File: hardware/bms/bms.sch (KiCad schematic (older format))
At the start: 159 parts

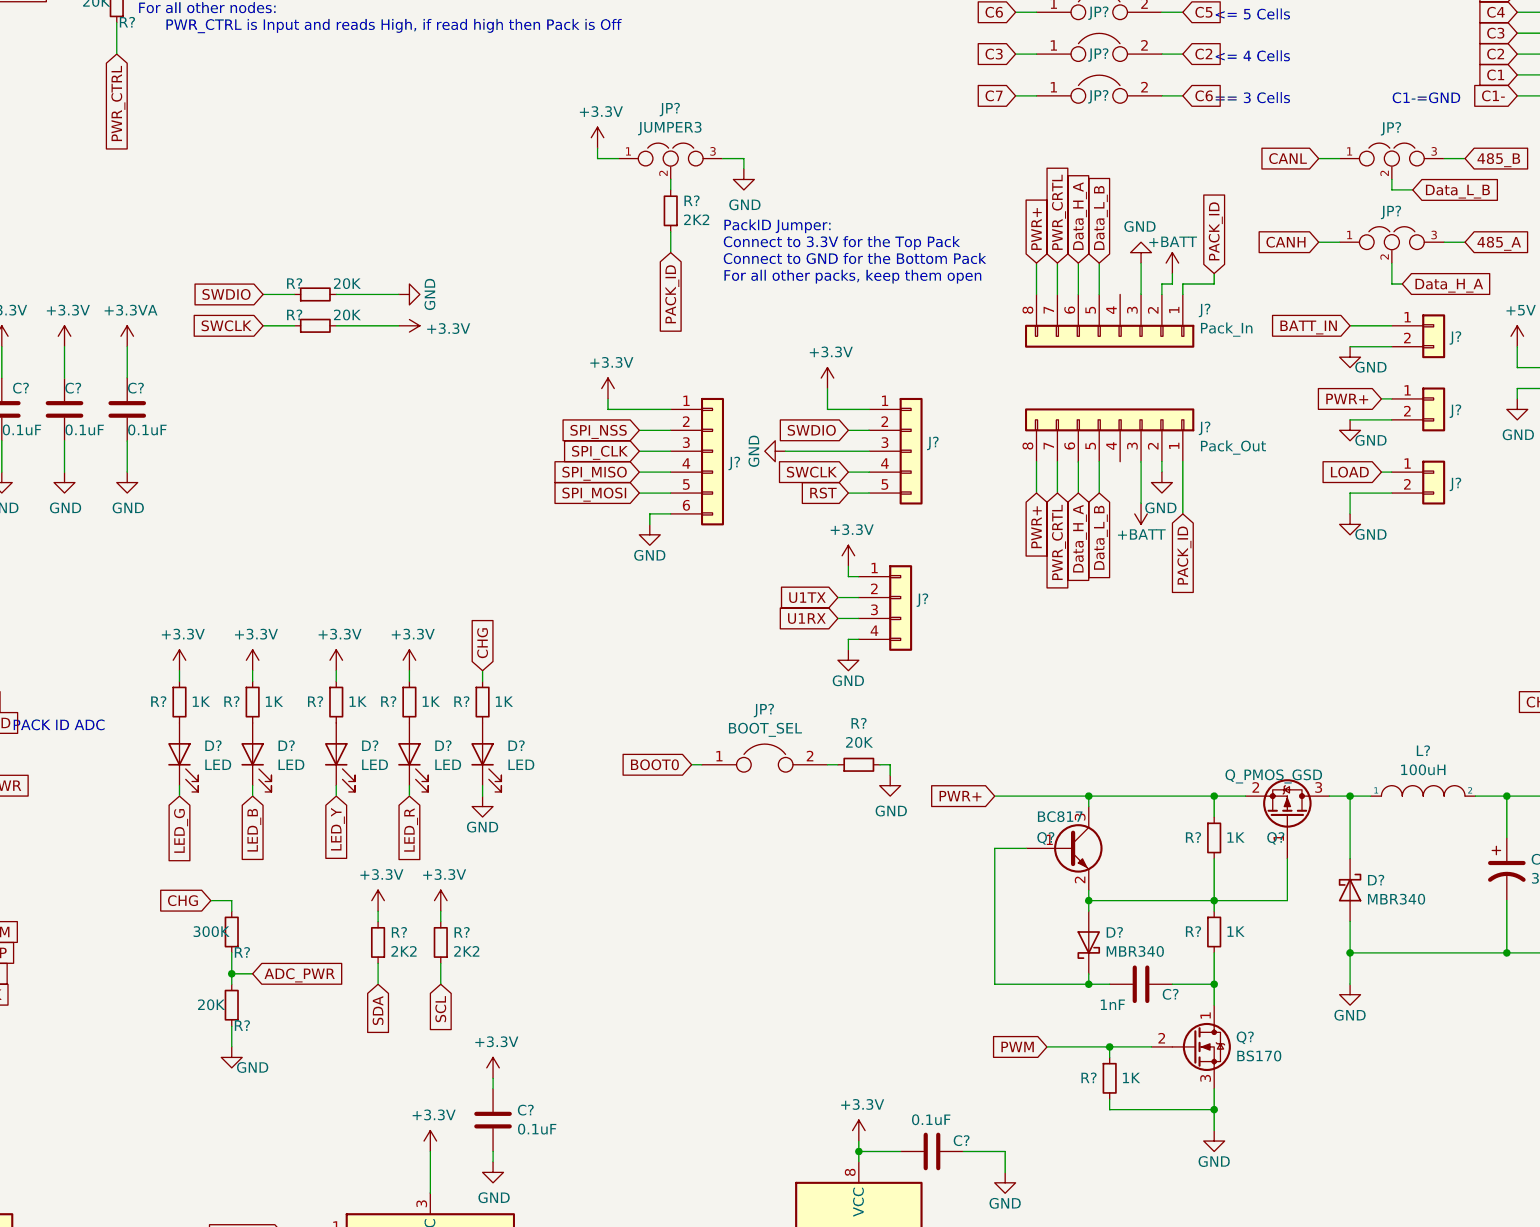
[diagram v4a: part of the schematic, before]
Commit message: changed the charger power connection, need to fix the power delivery logic
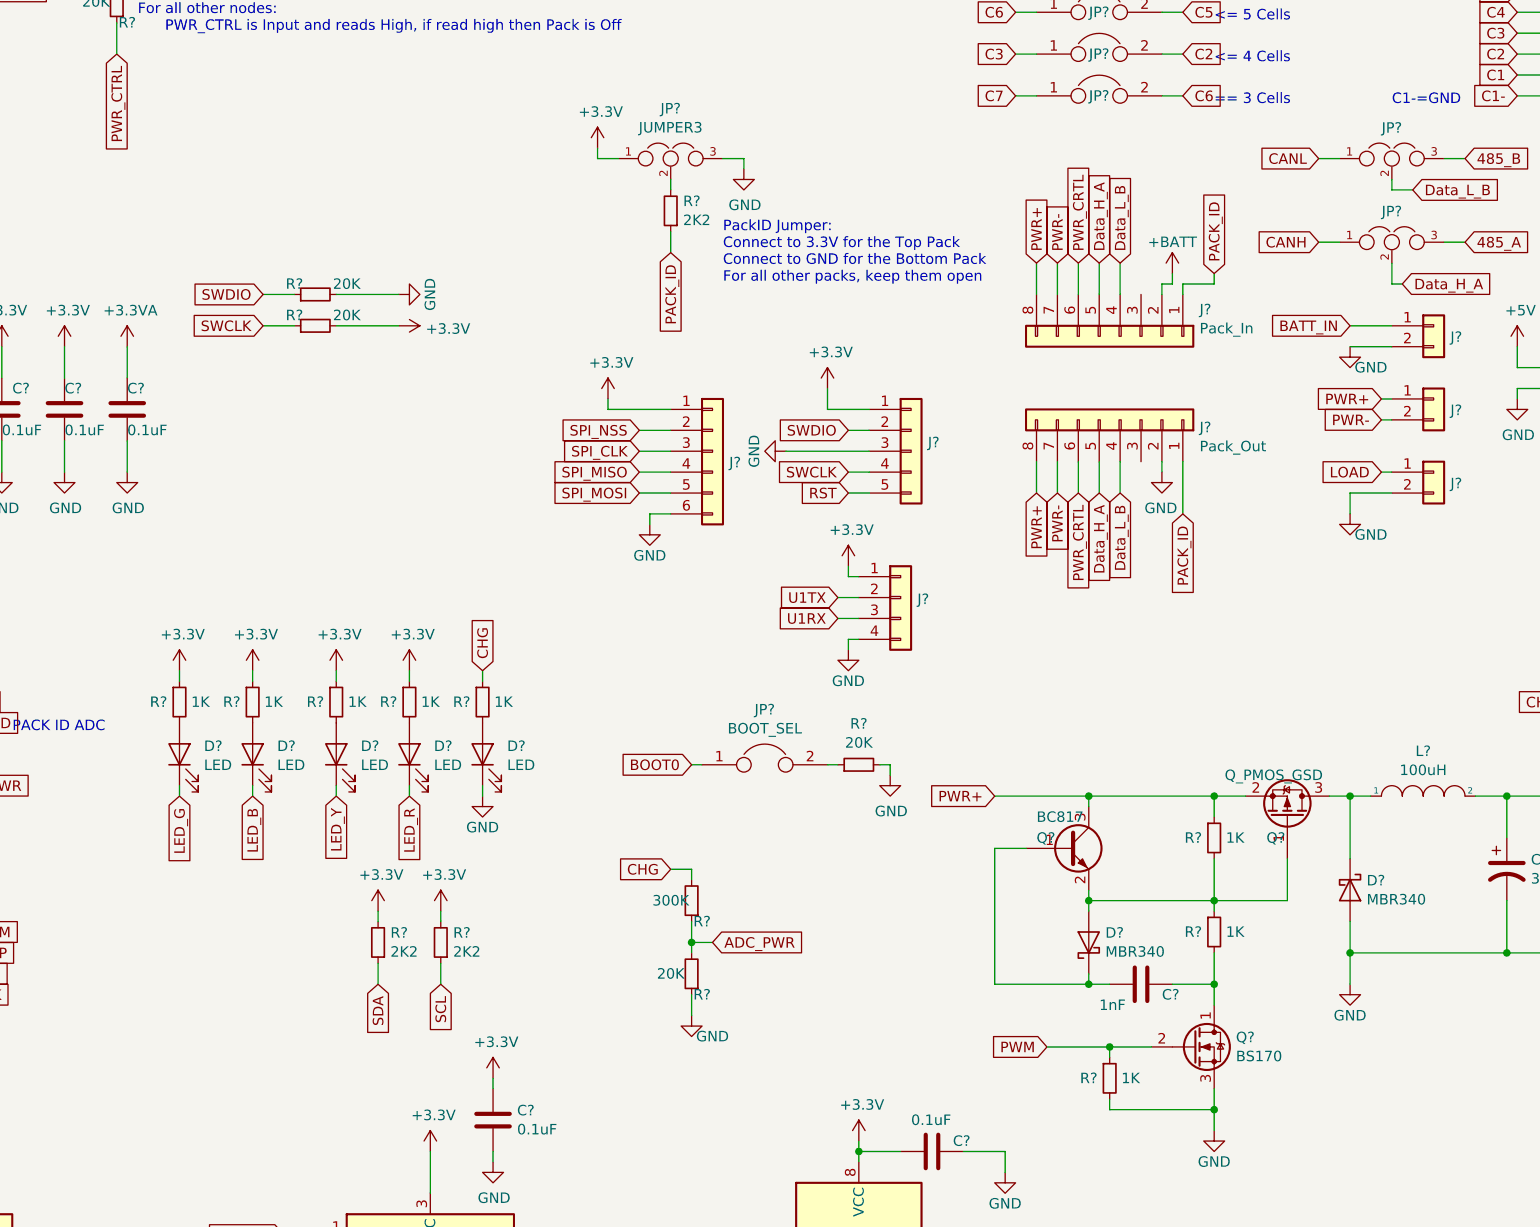
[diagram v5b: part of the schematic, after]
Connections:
- net +BATT: no longer J?.3 (Pin_3)
- net Data_H_A: now also J?.5 (Pin_5), J?.5 (Pin_5); no longer J?.6 (Pin_6), J?.6 (Pin_6)
- net Data_L_B: now also J?.4 (Pin_4), J?.4 (Pin_4); no longer J?.5 (Pin_5), J?.5 (Pin_5)
- net GND: no longer J?.2 (Pin_2), J?.3 (Pin_3)
- net PWR_CRTL: now also J?.6 (Pin_6), J?.6 (Pin_6); no longer J?.7 (Pin_7), J?.7 (Pin_7)
- new net PWR-: J?.2 (Pin_2), J?.7 (Pin_7), J?.7 (Pin_7)
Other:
- moved on the sheet: R?
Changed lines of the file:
@@
 Wire Wire Line
 	9900 6350 9900 6450
-Wire Wire Line
-	10100 6000 9900 6000
 Text GLabel 10700 4450 0    50   Input ~ 0
 C1-
@@
 $Comp
 L power:GND #PWR?
-U 1 1 5EBE5BFE
-P 9900 6000
-F 0 "#PWR?" H 9900 5750 50  0001 C CNN
-F 1 "GND" H 10000 5900 50  0000 C CNN
-F 2 "" H 9900 6000 50  0001 C CNN
-F 3 "" H 9900 6000 50  0001 C CNN
-	1    9900 6000
-	1    0    0    -1
-$EndComp
-$Comp
-L power:GND #PWR?
 U 1 1 5EBE5F36
 P 9900 5650
@@
 L Device:R_Small R?
 U 1 1 5F1259BA
-P 4550 8450
-F 0 "R?" H 4500 8550 50  0000 C CNN
-F 1 "300K" H 4650 8450 50  0000 C CNN
-F 2 "Resistor_SMD:R_0603_1608Metric_Pad1.05x0.95mm_HandSolder" H 4550 8450 50  0001 C CNN
-F 3 "~" H 4550 8450 50  0001 C CNN
-	1    4550 8450
+P 6750 8300
+F 0 "R?" H 6700 8400 50  0000 C CNN
+F 1 "300K" H 6850 8300 50  0000 C CNN
+F 2 "Resistor_SMD:R_0603_1608Metric_Pad1.05x0.95mm_HandSolder" H 6750 8300 50  0001 C CNN
+F 3 "~" H 6750 8300 50  0001 C CNN
+	1    6750 8300
 	-1   0    0    1
 $EndComp
@@
 L Device:R_Small R?
 U 1 1 5F1264EC
-P 4550 8800
-F 0 "R?" H 4500 8900 50  0000 C CNN
-F 1 "20K" H 4650 8800 50  0000 C CNN
-F 2 "Resistor_SMD:R_0603_1608Metric_Pad1.05x0.95mm_HandSolder" H 4550 8800 50  0001 C CNN
-F 3 "~" H 4550 8800 50  0001 C CNN
-	1    4550 8800
+P 6750 8650
+F 0 "R?" H 6700 8750 50  0000 C CNN
+F 1 "20K" H 6850 8650 50  0000 C CNN
+F 2 "Resistor_SMD:R_0603_1608Metric_Pad1.05x0.95mm_HandSolder" H 6750 8650 50  0001 C CNN
+F 3 "~" H 6750 8650 50  0001 C CNN
+	1    6750 8650
 	-1   0    0    1
 $EndComp
-Text GLabel 4450 8300 0    50   Input ~ 0
+Text GLabel 6650 8150 0    50   Input ~ 0
 CHG
 Wire Wire Line
-	4450 8300 4550 8300
-Wire Wire Line
-	4550 8300 4550 8350
-Wire Wire Line
-	4550 8550 4550 8650
+	6650 8150 6750 8150
+Wire Wire Line
+	6750 8150 6750 8200
+Wire Wire Line
+	6750 8400 6750 8500
 $Comp
 L power:GND #PWR?
 U 1 1 5F1AA8E9
-P 4550 9000
-F 0 "#PWR?" H 4550 8750 50  0001 C CNN
-F 1 "GND" H 4650 8900 50  0000 C CNN
-F 2 "" H 4550 9000 50  0001 C CNN
-F 3 "" H 4550 9000 50  0001 C CNN
-	1    4550 9000
-	1    0    0    -1
-$EndComp
-Wire Wire Line
-	4550 8900 4550 9000
-Text GLabel 4650 8650 2    50   Input ~ 0
+P 6750 8850
+F 0 "#PWR?" H 6750 8600 50  0001 C CNN
+F 1 "GND" H 6850 8750 50  0000 C CNN
+F 2 "" H 6750 8850 50  0001 C CNN
+F 3 "" H 6750 8850 50  0001 C CNN
+	1    6750 8850
+	1    0    0    -1
+$EndComp
+Wire Wire Line
+	6750 8750 6750 8850
+Text GLabel 6850 8500 2    50   Input ~ 0
 ADC_PWR
 Wire Wire Line
-	4650 8650 4550 8650
-Connection ~ 4550 8650
-Wire Wire Line
-	4550 8650 4550 8700
+	6850 8500 6750 8500
+Connection ~ 6750 8500
+Wire Wire Line
+	6750 8500 6750 8550
 Text GLabel 9250 5300 1    50   Input ~ 0
 PACK_ID
@@
 Text GLabel 8400 6350 3    50   Input ~ 0
 PWR+
-$Comp
-L power:+BATT #PWR?
-U 1 1 5F32C9B6
-P 8900 6400
-F 0 "#PWR?" H 8900 6250 50  0001 C CNN
-F 1 "+BATT" H 8900 6550 50  0000 C CNN
-F 2 "" H 8900 6400 50  0001 C CNN
-F 3 "" H 8900 6400 50  0001 C CNN
-	1    8900 6400
-	1    0    0    1
-$EndComp
 $Comp
 L power:GND #PWR?
@@
 Wire Wire Line
 	9250 5350 9250 5300
-$Comp
-L power:GND #PWR?
-U 1 1 5F328E25
-P 8900 5250
-F 0 "#PWR?" H 8900 5000 50  0001 C CNN
-F 1 "GND" H 8905 5077 50  0000 C CNN
-F 2 "" H 8900 5250 50  0001 C CNN
-F 3 "" H 8900 5250 50  0001 C CNN
-	1    8900 5250
-	-1   0    0    1
-$EndComp
-Wire Wire Line
-	8900 5250 8900 5400
-Text GLabel 8600 5250 1    50   Input ~ 0
+Text GLabel 8700 5250 1    50   Input ~ 0
 Data_H_A
-Text GLabel 8700 5250 1    50   Input ~ 0
+Text GLabel 8800 5250 1    50   Input ~ 0
 Data_L_B
-Wire Wire Line
-	8900 6200 8900 6400
 $Comp
 L Connector_Generic:Conn_01x08 J?
@@
 $EndComp
 Wire Wire Line
-	8600 5250 8600 5400
-Wire Wire Line
 	8700 5250 8700 5400
 Wire Wire Line
+	8800 5250 8800 5400
+Wire Wire Line
 	9000 6200 9000 6250
 Wire Wire Line
@@
 Wire Wire Line
 	8400 6350 8400 6200
-Text GLabel 8600 6350 3    50   Input ~ 0
+Text GLabel 8700 6350 3    50   Input ~ 0
 Data_H_A
-Text GLabel 8700 6350 3    50   Input ~ 0
+Text GLabel 8800 6350 3    50   Input ~ 0
 Data_L_B
 Wire Wire Line
-	8600 6200 8600 6350
-Wire Wire Line
 	8700 6200 8700 6350
+Wire Wire Line
+	8800 6200 8800 6350
 Wire Wire Line
 	8400 5250 8400 5400
@@
 Wire Wire Line
 	1400 8450 1750 8450
-Text GLabel 8500 6350 3    50   Input ~ 0
+Text GLabel 8600 6350 3    50   Input ~ 0
 PWR_CRTL
 Wire Wire Line
-	8500 6200 8500 6350
-Text GLabel 8500 5250 1    50   Input ~ 0
+	8600 6200 8600 6350
+Text GLabel 8600 5250 1    50   Input ~ 0
 PWR_CRTL
 Wire Wire Line
-	8500 5250 8500 5400
+	8600 5250 8600 5400
 Text Notes 6900 5350 0    50   ~ 0
 PackID Jumper:\nConnect to 3.3V for the Top Pack\nConnect to GND for the Bottom Pack\nFor all other packs, keep them open
@@
 Wire Wire Line
 	3100 1950 3300 1950
+Wire Wire Line
+	8500 5250 8500 5400
+Wire Wire Line
+	8500 6350 8500 6200
+Text GLabel 8500 6350 3    50   Input ~ 0
+PWR-
+Text GLabel 8500 5250 1    50   Input ~ 0
+PWR-
+Wire Wire Line
+	10050 6000 10100 6000
+Text GLabel 10050 6000 0    50   Input ~ 0
+PWR-
 $EndSCHEMATC
